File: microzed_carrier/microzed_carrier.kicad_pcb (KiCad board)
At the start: 2 copper layers, 2 parts, among them P1 61083-101400LF, P2 61083-101400LF

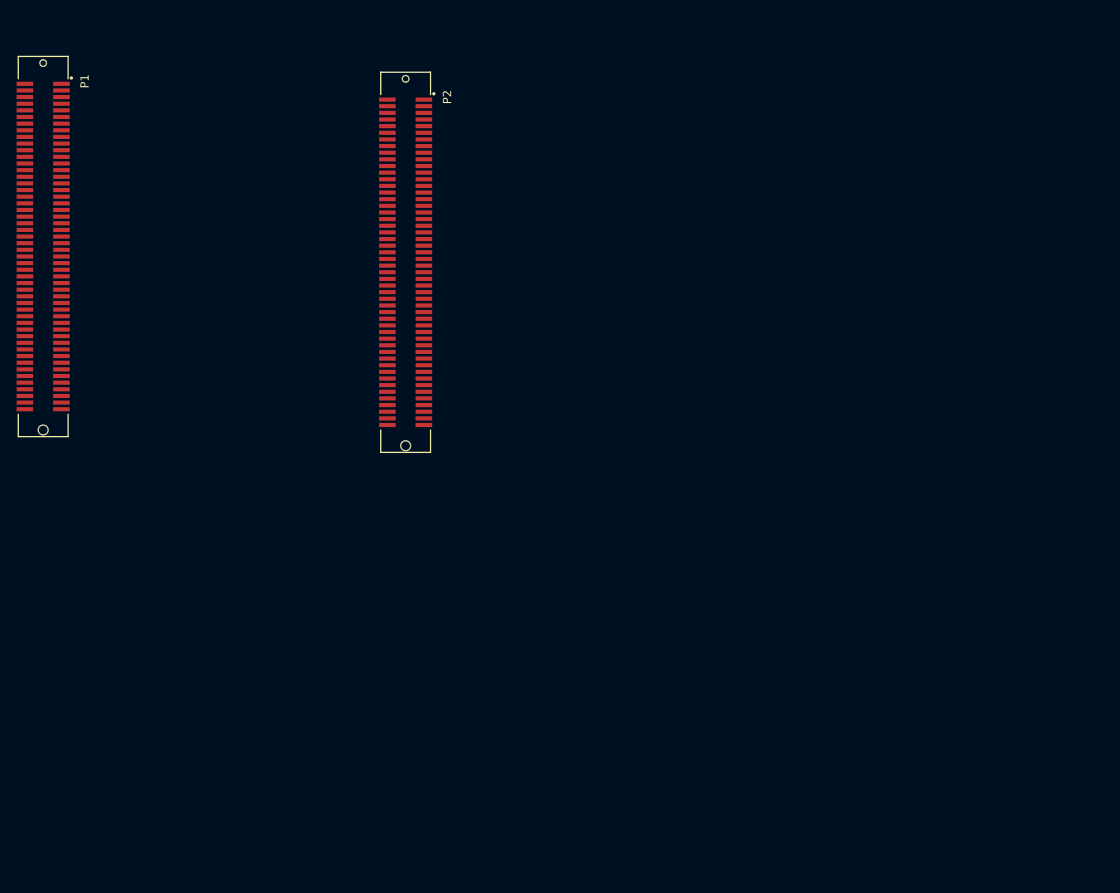
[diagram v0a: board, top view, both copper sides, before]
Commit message: added microzed outline and mounting holes
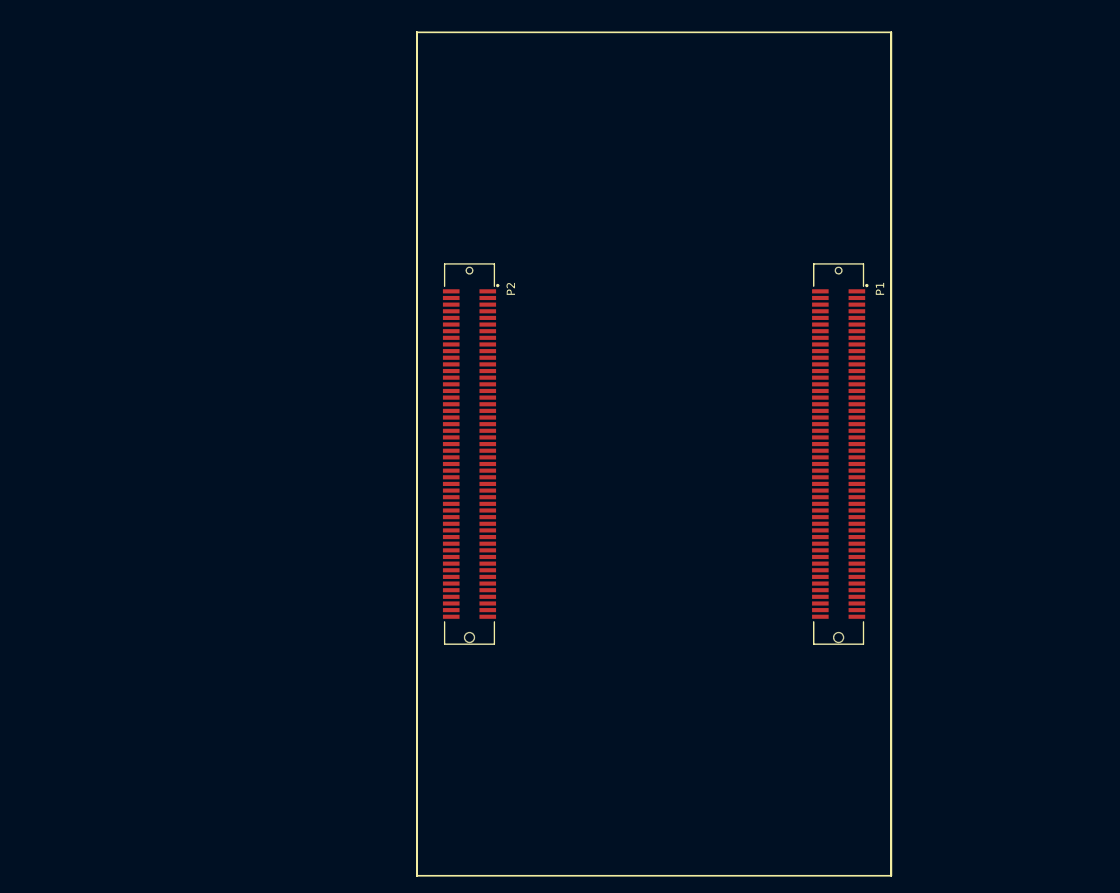
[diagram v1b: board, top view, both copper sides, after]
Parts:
- moved P1 99.0 mm to (149.2, 101.6)
- moved P2 24.3 mm to (104.8, 101.6)
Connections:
- P1 pad 15: unconnected-(P1-Pad15) -> GND
- P1 pad 16: unconnected-(P1-Pad16) -> GND
- P1 pad 21: unconnected-(P1-Pad21) -> GND
- P1 pad 22: unconnected-(P1-Pad22) -> GND
- P1 pad 27: unconnected-(P1-Pad27) -> GND
- P1 pad 28: unconnected-(P1-Pad28) -> GND
- P1 pad 33: unconnected-(P1-Pad33) -> GND
- P1 pad 34: unconnected-(P1-Pad34) -> GND
- P1 pad 39: unconnected-(P1-Pad39) -> GND
- P1 pad 40: unconnected-(P1-Pad40) -> GND
- P1 pad 45: unconnected-(P1-Pad45) -> GND
- P1 pad 46: unconnected-(P1-Pad46) -> GND
- P1 pad 51: unconnected-(P1-Pad51) -> GND
- P1 pad 52: unconnected-(P1-Pad52) -> GND
- P1 pad 57: unconnected-(P1-Pad57) -> /VIN_HDR
- P1 pad 58: unconnected-(P1-Pad58) -> /VIN_HDR
- P1 pad 59: unconnected-(P1-Pad59) -> /VIN_HDR
- P1 pad 60: unconnected-(P1-Pad60) -> /VIN_HDR
- P1 pad 65: unconnected-(P1-Pad65) -> GND
- P1 pad 66: unconnected-(P1-Pad66) -> GND
- P1 pad 71: unconnected-(P1-Pad71) -> GND
- P1 pad 72: unconnected-(P1-Pad72) -> GND
- P1 pad 77: unconnected-(P1-Pad77) -> GND
- P1 pad 85: unconnected-(P1-Pad85) -> GND
- P1 pad 86: unconnected-(P1-Pad86) -> GND
- P1 pad 95: unconnected-(P1-Pad95) -> GND
- P1 pad 96: unconnected-(P1-Pad96) -> GND
- P2 pad 10: unconnected-(P2-Pad10) -> /VCCIO_EN
- P2 pad 11: unconnected-(P2-Pad11) -> /PG_MODULE
- P2 pad 12: unconnected-(P2-Pad12) -> /VIN_HDR
- P2 pad 15: unconnected-(P2-Pad15) -> GND
- P2 pad 16: unconnected-(P2-Pad16) -> GND
- P2 pad 21: unconnected-(P2-Pad21) -> GND
- P2 pad 22: unconnected-(P2-Pad22) -> GND
- P2 pad 27: unconnected-(P2-Pad27) -> GND
- P2 pad 28: unconnected-(P2-Pad28) -> GND
- P2 pad 33: unconnected-(P2-Pad33) -> GND
- P2 pad 34: unconnected-(P2-Pad34) -> GND
- P2 pad 39: unconnected-(P2-Pad39) -> GND
- P2 pad 40: unconnected-(P2-Pad40) -> GND
- P2 pad 45: unconnected-(P2-Pad45) -> GND
- P2 pad 46: unconnected-(P2-Pad46) -> GND
- P2 pad 51: unconnected-(P2-Pad51) -> GND
- P2 pad 52: unconnected-(P2-Pad52) -> GND
- P2 pad 57: unconnected-(P2-Pad57) -> /VIN_HDR
- P2 pad 58: unconnected-(P2-Pad58) -> /VIN_HDR
- P2 pad 59: unconnected-(P2-Pad59) -> /VIN_HDR
- P2 pad 60: unconnected-(P2-Pad60) -> /VIN_HDR
- P2 pad 65: unconnected-(P2-Pad65) -> GND
- P2 pad 66: unconnected-(P2-Pad66) -> GND
- P2 pad 71: unconnected-(P2-Pad71) -> GND
- P2 pad 72: unconnected-(P2-Pad72) -> GND
- P2 pad 77: unconnected-(P2-Pad77) -> GND
- P2 pad 85: unconnected-(P2-Pad85) -> GND
- P2 pad 86: unconnected-(P2-Pad86) -> GND
- P2 pad 95: unconnected-(P2-Pad95) -> GND
- P2 pad 96: unconnected-(P2-Pad96) -> GND

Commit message: added mounting holes and some LEDs
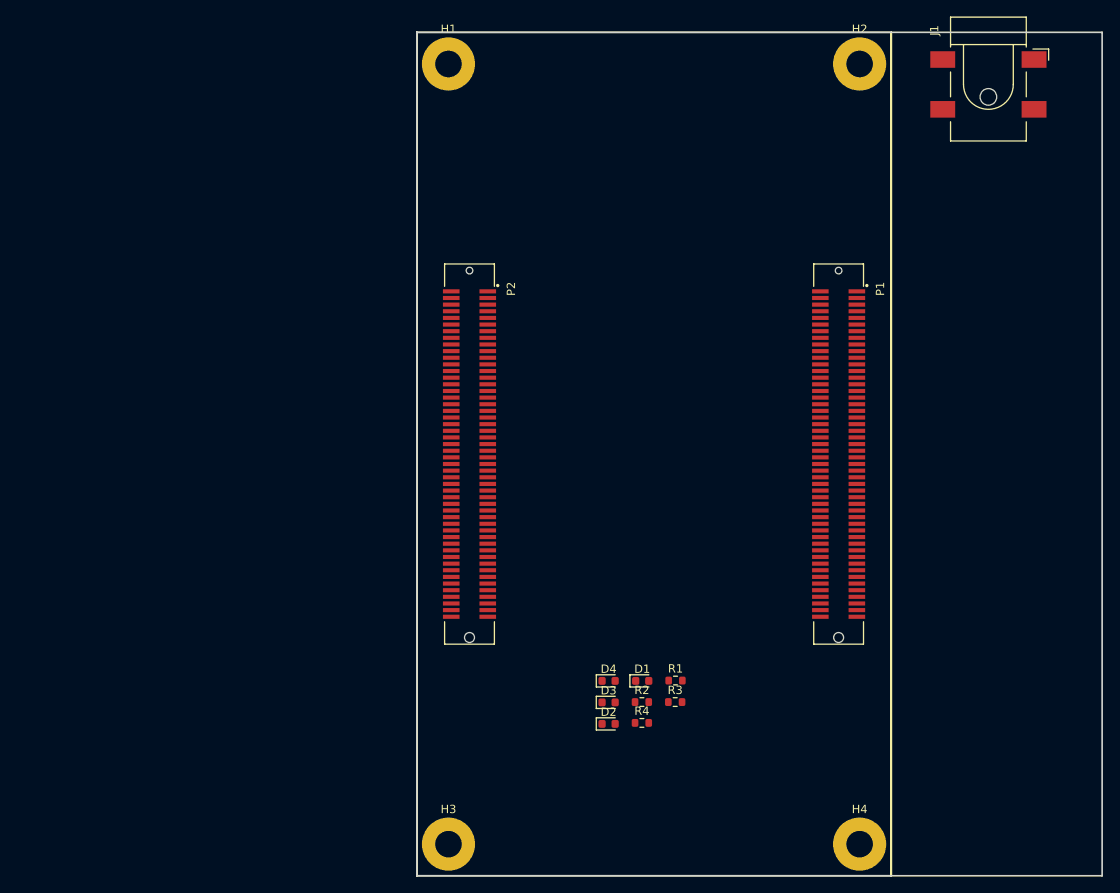
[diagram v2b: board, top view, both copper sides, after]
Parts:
- added D1: LED, LED_SMD:LED_0603_1608Metric, F.Cu at (125.6, 128.9)
- added D2: LED, LED_SMD:LED_0603_1608Metric, F.Cu at (121.5, 134.1)
- added D3: LED, LED_SMD:LED_0603_1608Metric, F.Cu at (121.5, 131.5)
- added D4: LED, LED_SMD:LED_0603_1608Metric, F.Cu at (121.5, 128.9)
- added H1: microzed_mount_hole, MountingHole:MountingHole_3.2mm_M3_Pad, F.Cu at (102.2, 54.6)
- added H2: microzed_mount_hole, MountingHole:MountingHole_3.2mm_M3_Pad, F.Cu at (151.8, 54.6)
- added H3: microzed_mount_hole, MountingHole:MountingHole_3.2mm_M3_Pad, F.Cu at (102.2, 148.6)
- added H4: microzed_mount_hole, MountingHole:MountingHole_3.2mm_M3_Pad, F.Cu at (151.8, 148.6)
- added J1: Jack-DC, Connector_BarrelJack:BarrelJack_CLIFF_FC681465S_SMT_Horizontal, F.Cu at (167.3, 57.1)
- added R1: R, Resistor_SMD:R_0603_1608Metric, F.Cu at (129.6, 128.9)
- added R2: R, Resistor_SMD:R_0603_1608Metric, F.Cu at (125.5, 131.5)
- added R3: R, Resistor_SMD:R_0603_1608Metric, F.Cu at (129.5, 131.5)
- added R4: R, Resistor_SMD:R_0603_1608Metric, F.Cu at (125.5, 134.0)
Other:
- board outline added: 82.5 x 101.6 mm
